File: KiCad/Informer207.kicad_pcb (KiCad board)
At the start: 2 copper layers, 42.8 x 53 mm, 24 parts, among them J1 PROG, J2 USB_B_Micro, J3 RS232, SW1 RESET, SW2 BOOT, U1 ESP32-WROOM-32, U2 MAX3232, U3 AMS1117-3.3

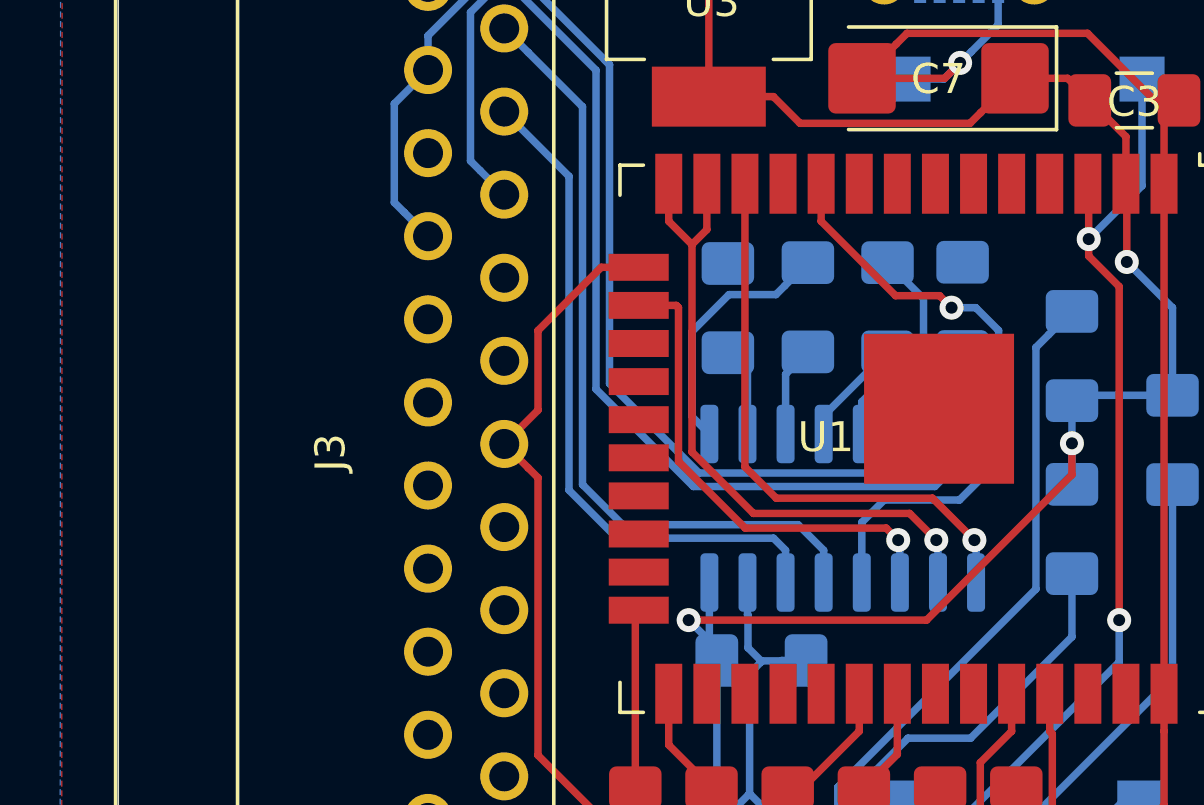
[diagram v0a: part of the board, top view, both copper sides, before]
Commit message: Added possible Ready To Recieve line (some activity on it)
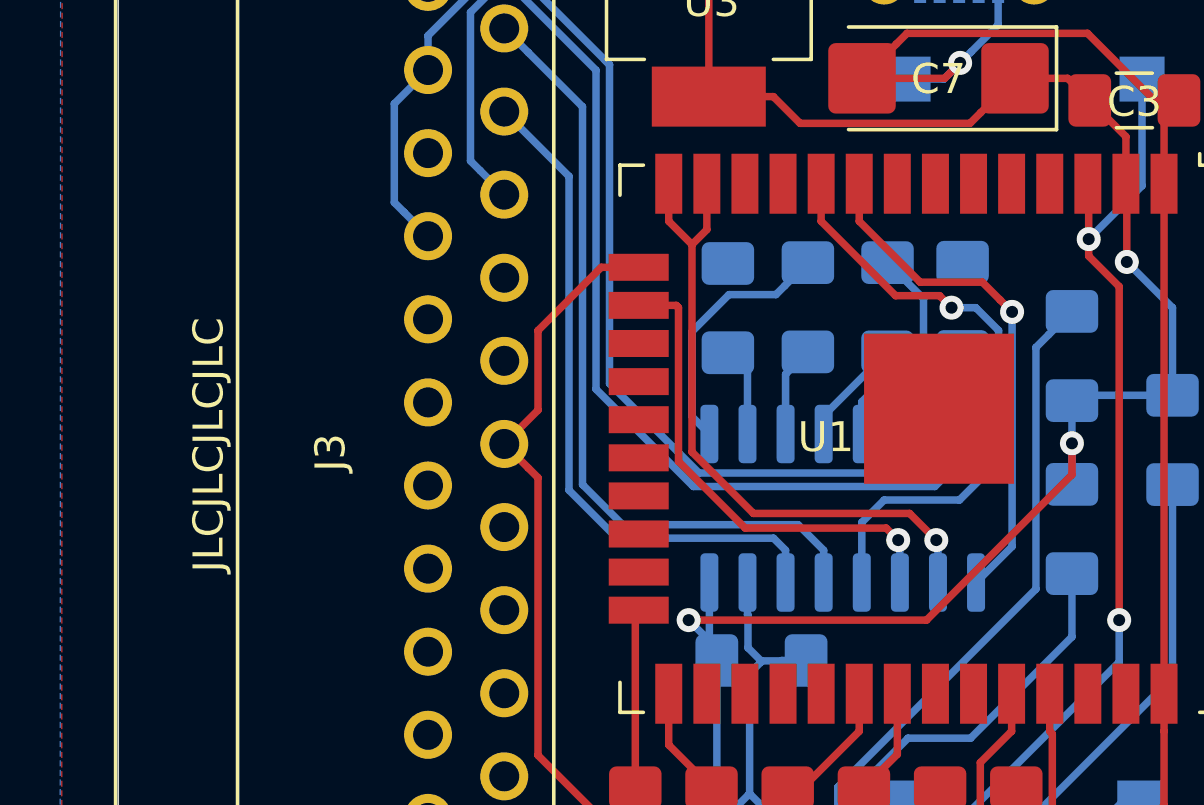
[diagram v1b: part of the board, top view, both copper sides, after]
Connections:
- U2 pad 9: Net-(U1-Pad12) -> Net-(U1-Pad9)
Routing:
- net Net-(U1-Pad12): track 19.5 -> 0.00 mm, vias 1 -> 0
- net Net-(U1-Pad9): track 0.00 -> 17.1 mm, vias 0 -> 1
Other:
- board text added: "JLCJLCJLCJLC"
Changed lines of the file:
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@@
   (general
     (thickness 1.6)
-    (drawings 27)
-    (tracks 281)
+    (drawings 28)
+    (tracks 282)
     (zones 0)
     (modules 24)
@@
     (visible_elements FFFFFF7F)
     (pcbplotparams
-      (layerselection 0x010fc_ffffffff)
+      (layerselection 0x010f0_ffffffff)
       (usegerberextensions false)
       (usegerberattributes false)
@@
       (outputformat 1)
       (mirror false)
-      (drillshape 1)
+      (drillshape 0)
       (scaleselection 1)
-      (outputdirectory ""))
+      (outputdirectory "Gerbers"))
   )
   (net 0 "")
@@
       (net 24 "Net-(J3-Pad4)"))
     (pad 9 smd roundrect (at 2.475 -4.445 270) (size 1.95 0.6) (layers B.Cu B.Paste B.Mask) (roundrect_rratio 0.25)
-      (net 57 "Net-(U1-Pad12)"))
+      (net 54 "Net-(U1-Pad9)"))
     (pad 10 smd roundrect (at 2.475 -3.175 270) (size 1.95 0.6) (layers B.Cu B.Paste B.Mask) (roundrect_rratio 0.25)
       (net 58 "Net-(U1-Pad13)"))
@@
       (rotate (xyz 0 0 0))
     )
+  )
+  (gr_text JLCJLCJLCJLC (at 137.16 105.41 90) (layer F.SilkS)
+    (effects (font (size 1 1) (thickness 0.15)))
   )
   (gr_text RECV (at 164.084 108.204 90) (layer B.SilkS)
@@
   (segment (start 158.8483 114.9568) (end 156.9651 116.84) (width 0.25) (layer F.Cu) (net 48))
   (segment (start 158.8483 113.7068) (end 158.8483 114.9568) (width 0.25) (layer F.Cu) (net 48))
+  (segment (start 162.743001 109.998901) (end 163.94332 108.798582) (width 0.25) (layer B.Cu) (net 54))
+  (via (at 163.94332 100.97868) (size 0.8) (drill 0.4) (layers F.Cu B.Cu) (net 54))
+  (segment (start 163.94332 108.798582) (end 163.94332 100.97868) (width 0.25) (layer B.Cu) (net 54))
+  (segment (start 162.952631 99.987991) (end 163.543321 100.578681) (width 0.25) (layer F.Cu) (net 54))
+  (segment (start 160.879491 99.987991) (end 162.952631 99.987991) (width 0.25) (layer F.Cu) (net 54))
+  (segment (start 163.543321 100.578681) (end 163.94332 100.97868) (width 0.25) (layer F.Cu) (net 54))
+  (segment (start 158.8483 97.9568) (end 160.879491 99.987991) (width 0.25) (layer F.Cu) (net 54))
+  (segment (start 158.8483 96.7068) (end 158.8483 97.9568) (width 0.25) (layer F.Cu) (net 54))
   (segment (start 162.73349 100.838) (end 161.925 100.838) (width 0.25) (layer B.Cu) (net 55))
   (segment (start 163.49331 101.59782) (end 162.73349 100.838) (width 0.25) (layer B.Cu) (net 55))
@@
   (segment (start 159.67967 107.24893) (end 158.933001 107.995599) (width 0.25) (layer B.Cu) (net 55))
   (segment (start 159.67967 107.24893) (end 162.18974 107.24893) (width 0.25) (layer B.Cu) (net 55))
-  (via (at 162.687 108.585) (size 0.8) (drill 0.4) (layers F.Cu B.Cu) (net 57))
-  (segment (start 162.743001 108.641001) (end 162.687 108.585) (width 0.25) (layer B.Cu) (net 57))
-  (segment (start 162.743001 109.998901) (end 162.743001 108.641001) (width 0.25) (layer B.Cu) (net 57))
-  (segment (start 162.687 108.585) (end 161.29 107.188) (width 0.25) (layer F.Cu) (net 57))
-  (segment (start 161.29 107.188) (end 156.083 107.188) (width 0.25) (layer F.Cu) (net 57))
-  (segment (start 155.0383 106.1433) (end 155.0383 96.7068) (width 0.25) (layer F.Cu) (net 57))
-  (segment (start 156.083 107.188) (end 155.0383 106.1433) (width 0.25) (layer F.Cu) (net 57))
   (via (at 161.417 108.585) (size 0.8) (drill 0.4) (layers F.Cu B.Cu) (net 58))
   (segment (start 161.473001 108.641001) (end 161.417 108.585) (width 0.25) (layer B.Cu) (net 58))
